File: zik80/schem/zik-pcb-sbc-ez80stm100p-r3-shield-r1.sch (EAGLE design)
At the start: 7 parts

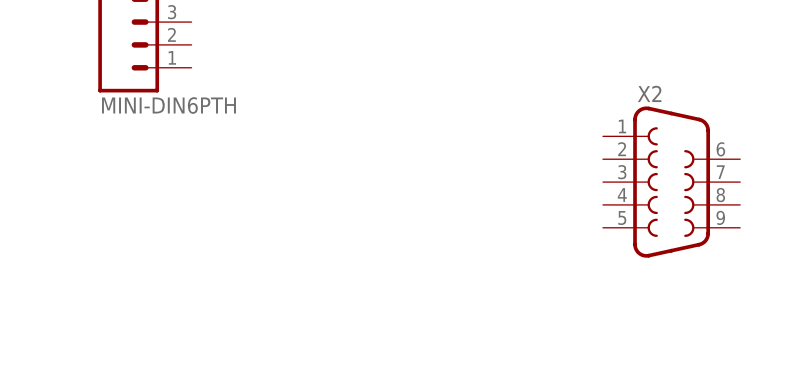
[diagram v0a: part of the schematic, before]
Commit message: Updated headphone part
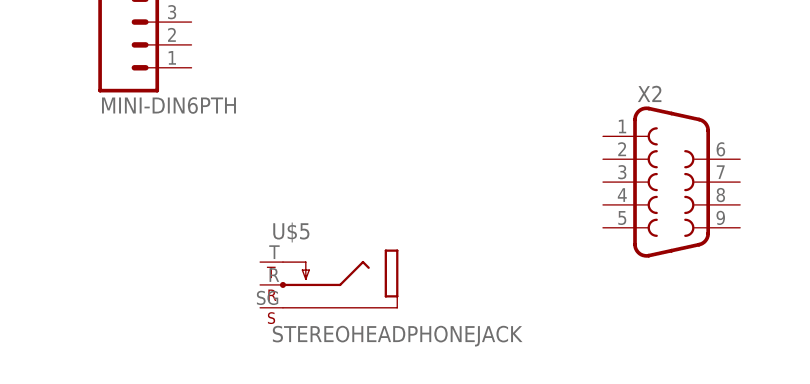
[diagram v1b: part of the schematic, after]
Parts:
- added U$5: STEREOHEADPHONEJACK, skeezix:STEREOHEADPHONEJACK
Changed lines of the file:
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@@
 <layer number="57" name="tCAD" color="10" fill="1" visible="no" active="no"/>
 <layer number="58" name="bCAD" color="11" fill="1" visible="no" active="no"/>
+<layer number="59" name="tCarbon" color="7" fill="1" visible="no" active="no"/>
+<layer number="60" name="bCarbon" color="7" fill="1" visible="no" active="no"/>
+<layer number="90" name="Modules" color="7" fill="1" visible="no" active="yes"/>
 <layer number="91" name="Nets" color="2" fill="1" visible="yes" active="yes"/>
 <layer number="92" name="Busses" color="1" fill="1" visible="yes" active="yes"/>
@@
 <layer number="127" name="_tValues" color="7" fill="1" visible="yes" active="yes"/>
 <layer number="128" name="_bValues" color="7" fill="1" visible="yes" active="yes"/>
+<layer number="129" name="Mask" color="7" fill="1" visible="yes" active="yes"/>
 <layer number="131" name="prix" color="7" fill="1" visible="yes" active="yes"/>
 <layer number="132" name="test" color="7" fill="1" visible="yes" active="yes"/>
@@
 <layer number="223" name="223bmp" color="24" fill="1" visible="no" active="no"/>
 <layer number="224" name="224bmp" color="25" fill="1" visible="no" active="no"/>
+<layer number="225" name="225bmp" color="7" fill="1" visible="yes" active="yes"/>
+<layer number="226" name="226bmp" color="7" fill="1" visible="yes" active="yes"/>
+<layer number="227" name="227bmp" color="7" fill="1" visible="yes" active="yes"/>
+<layer number="228" name="228bmp" color="7" fill="1" visible="yes" active="yes"/>
+<layer number="229" name="229bmp" color="7" fill="1" visible="yes" active="yes"/>
+<layer number="230" name="230bmp" color="7" fill="1" visible="yes" active="yes"/>
 <layer number="231" name="Eagle3D_PG1" color="7" fill="1" visible="yes" active="yes"/>
 <layer number="232" name="Eagle3D_PG2" color="7" fill="1" visible="yes" active="yes"/>
@@
 <layer number="251" name="SMDround" color="12" fill="11" visible="no" active="no"/>
 <layer number="254" name="cooling" color="7" fill="1" visible="yes" active="yes"/>
+<layer number="255" name="routoute" color="7" fill="1" visible="yes" active="yes"/>
 </layers>
 <schematic xreflabel="%F%N/%S.%C%R" xrefpart="/%S.%C%R">
@@
 <part name="VGA1" library="VideoConnectors-skeemod" deviceset="VGA-*" device="F90B"/>
 <part name="X1" library="adafruit-musb-skeemod" deviceset="USB" device="MICRO_20329"/>
+<part name="U$5" library="skeezix" deviceset="STEREOHEADPHONEJACK" device=""/>
 </parts>
 <sheets>
@@
 <instance part="VGA1" gate="G$1" x="157.48" y="66.04"/>
 <instance part="X1" gate="G$1" x="38.1" y="66.04"/>
+<instance part="U$5" gate="G$1" x="101.6" y="-7.62"/>
 </instances>
 <busses>
@@
 </schematic>
 </drawing>
+<compatibility>
+<note version="6.3" minversion="6.2.2" severity="warning">
+Since Version 6.2.2 text objects can contain more than one line,
+which will not be processed correctly with this version.
+</note>
+</compatibility>
 </eagle>

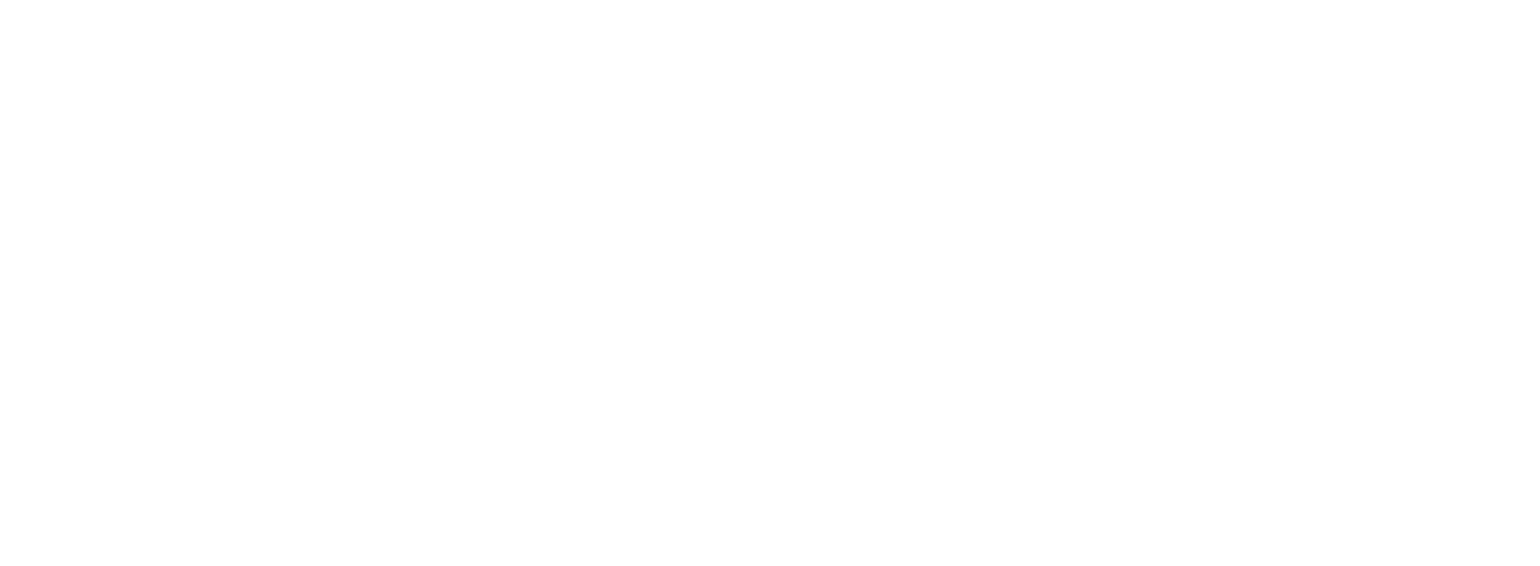
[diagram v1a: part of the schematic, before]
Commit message: Dropped TPS7133QP and FTDI onto shield start
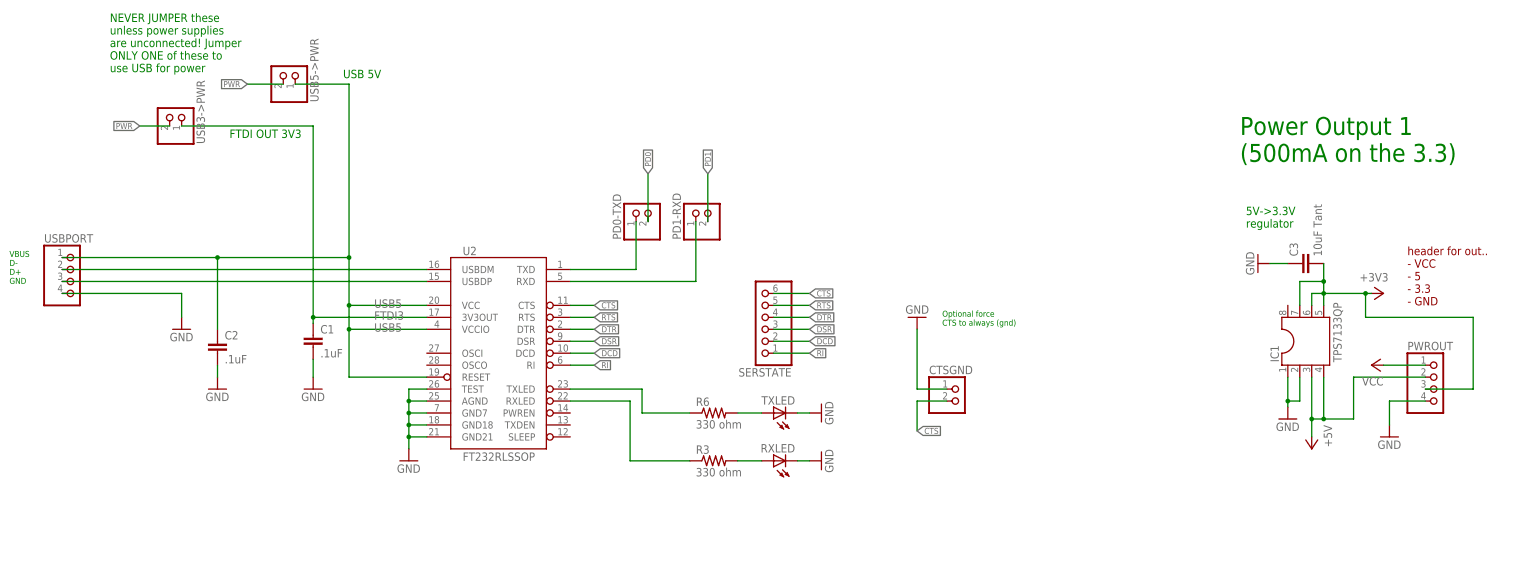
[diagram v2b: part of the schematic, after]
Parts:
- added C1, C2: .1uF, rcl:C-EU025-025X050
- added C3: 10uF Tant, rcl:C-EU025-025X050
- added CTSGND, PD0-TXD, PD1-RXD, USB3->PWR, USB5->PWR: (no value), pinhead:PINHD-1X2
- added IC1: TPS7133QP, ic-package:DIL8
- added PWROUT, USBPORT: (no value), pinhead:PINHD-1X4
- added R3, R6: 330 ohm, rcl:R-US_0204/7
- added RXLED, TXLED: (no value), SparkFun-LED:LED5MM
- added SERSTATE: (no value), pinhead:PINHD-1X6
- added U2: FT232RLSSOP, SparkFun:FT232RLSSOP
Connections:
- new net +3V3: C3.2, IC1.5, IC1.6, IC1.7, PWROUT.3
- new net +5V: IC1.3, IC1.4, PWROUT.2
- new net CTS: CTSGND.2, SERSTATE.6, U2.CTS
- new net DCD: SERSTATE.2, U2.DCD
- new net DSR: SERSTATE.3, U2.DSR
- new net DTR: SERSTATE.4, U2.DTR
- new net FTDI3: C1.1, U2.3V3OUT, USB3->PWR.1
- new net GND: C1.2, C2.2, C3.1, CTSGND.1, IC1.1, IC1.2, PWROUT.4, RXLED.C, TXLED.C, U2.AGND, U2.GND18, U2.GND21, U2.GND7, U2.TEST, USBPORT.4
- new net N$10: R3.2, RXLED.A
- new net N$11: R3.1, U2.RXLED
- new net N$12: PD0-TXD.1, U2.TXD
- new net N$13: PD1-RXD.1, U2.RXD
- new net N$4: R6.2, TXLED.A
- new net N$8: R6.1, U2.TXLED
- new net PD0: PD0-TXD.2
- new net PD1: PD1-RXD.2
- new net PWR: USB3->PWR.2, USB5->PWR.2
- new net RI: SERSTATE.1, U2.RI
- new net RTS: SERSTATE.5, U2.RTS
- new net USB5: C2.1, U2.RESET, U2.VCC, U2.VCCIO, USB5->PWR.1, USBPORT.1
- new net USB_D+: U2.USBDP, USBPORT.3
- new net USB_D-: U2.USBDM, USBPORT.2
- new net VCC: PWROUT.1
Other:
- note added: "5V->3.3V regulator"
- note added: "FTDI OUT 3V3"
- note added: "NEVER JUMPER these unless power supplies are unconnected! Jumper ONLY ONE of these to use USB for power"
- note added: "Optional force CTS to always (gnd)"
- note added: "Power Output 1 (500mA on the 3.3)"
- note added: "USB 5V"
- note added: "VBUS D- D+ GND"
- note added: "header for out.. - VCC - 5 - 3.3 - GND"

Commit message: shield progress.. about 50%? pcb coming together, working on placement. Schem has most or everything, just need to hook it all up.
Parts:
- removed X1: (no value), adafruit-musb-skeemod:USBMICRO_20329
- removed X2: (no value), SparkFun-Connectors-skeemod:DB9FEMALE
- added 3V3OUT, 5OUT, GNDOUT: (no value), pinhead:PINHD-1X3
- added BOB-PA: (no value), pinhead:PINHD-1X16
- added BOBGPIOB, GPIOC-JOY0, GPIOD-JOY1: (no value), pinhead:PINHD-1X8
- added C23: 100uF, rcl:C-EU025-025X050
- added C25: 250uF Pol, rcl:CPOL-USE3.5-8
- added C26: .05uF, rcl:C-EU025-025X050
- added JOY0, JOY1: (no value), SparkFun-Connectors-skeemod:DB9FEMALE
- added LINEOUT: (no value), pinhead:PINHD-1X2
- added PS2KEYB, PWRIN, SPKR: (no value), pinhead:PINHD-1X4
- added R34: 1K, rcl:R-US_0204/7
- added R37: 10, rcl:R-US_0204/7
- added U$6: LM386-DIP, skeezix:LM386-DIP
- added USBGPU, USBSERPWR: (no value), adafruit-musb-skeemod:USBMICRO_20329
- added VGAHDR: (no value), pinhead:PINHD-1X6
- renumbered PD0-TXD to ZPD1-TXD, PD1-RXD to ZPD0-RXD, USB3->PWR to FT3V3->PWR3, USB5->PWR to FT5V->PWR5
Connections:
- removed net +3V3: C3.2, IC1.5, IC1.6, IC1.7, PWROUT.3
- removed net PD0: ZPD1-TXD.2
- removed net PD1: ZPD0-RXD.2
- removed net PWR: FT3V3->PWR3.2, FT5V->PWR5.2
- new net N$1: C23.2, U$3.CCW
- new net N$2: U$3.LO, U$6.3
- new net N$22: C25.+, C26.2, U$6.5
- new net N$23: C25.-
- new net N$24: C26.1, R37.2
- new net N$3: LINEOUT.2, U$6.7
- new net N$6: C23.1, R34.1, SPKR.1, SPKR.2, SPKR.3
- new net PWR3: 3V3OUT.1, 3V3OUT.2, 3V3OUT.3, C3.2, FT3V3->PWR3.2, IC1.5, IC1.6, IC1.7, PWRIN.3, PWROUT.3
- new net PWR5: 5OUT.1, 5OUT.2, 5OUT.3, FT5V->PWR5.2, IC1.3, IC1.4, PWRIN.2, PWROUT.2, U$1.VCC
- new net SPA0: BOB-PA.1
- new net SPA10: BOB-PA.11
- new net SPA11: BOB-PA.12, USBGPU.D-
- new net SPA12: BOB-PA.13, USBGPU.D+
- new net ZPB0: BOBGPIOB.1
- new net ZPB2-SS: BOBGPIOB.3
- new net ZPB3-SCK: BOBGPIOB.4
- new net ZPB6-MISO: BOBGPIOB.7
- new net ZPB7-MOSI: BOBGPIOB.8
- new net ZPD0: GPIOD-JOY1.1, ZPD0-RXD.2
- new net ZPD1: GPIOD-JOY1.2, ZPD1-TXD.2
- new net ZPD6: GPIOD-JOY1.7
- new net ZPD7: GPIOD-JOY1.8
- net +5V: now also U$6.6, USBGPU.VBUS; no longer IC1.3, IC1.4, PWROUT.2
- net GND: now also GNDOUT.1, GNDOUT.2, GNDOUT.3, LINEOUT.1, PWRIN.4, R34.2, R37.1, U$1.GND, U$3.CW, U$6.2, U$6.4, USBGPU.GND, USBSERPWR.GND
- net USB5: now also USBSERPWR.VBUS
- net USB_D+: now also USBSERPWR.D-
- net USB_D-: now also USBSERPWR.D+
- net VCC: now also PWRIN.1
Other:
- note added: "- NEVER JUMPER enable these unless barrel power jack or headers are unconnected! - Jumper ONLY ONE of these to use USB for power"
- note added: "Audio Amp"
- note added: "FTDI RX -> mcu TX"
- note added: "FTDI TX -> mcu RX"
- note added: "OTG_FS_ID OTG_FS_DM OTG_FS_DP"
- note added: "One of: - USB jack, then jumper enable 5v (populated TPS7133) - USB jack, jumper enable 5v and 3v3v (unpopulated TPS7133); pray FTDI can supply enough amp on 3V line - Barrel jack with 5V input brick (populated TPS7133) .. needs TPS - PWRIN header with VCC, 5V, 3V3, GND (unpopulated TPS7133) .. circumvents TPS"
- note added: "Power Block"
- note added: "Powering PCB Notes"
- note added: "Use Vcc12V or +5? Decouple Vcc/GND with a cap?"
- note added: "VCC 5V 3V3 GND"
- note added: "Verify - all pin1 orientations! - which jacks can be used, while in middle of pcb - jacks in middle have clearance for SD-pulling, headphone pulling, etc - ensure cap, resistor sizine/type - printout pcb to printer, eyeball it - PWR v PW% vs PWR3 vs 5V vs etc .. all powers are hooked right - net review; ensure no +5V and other old net names - uncover reset buttons.. anything else? LEDs? - verify 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"
- note added: "joy up (z80 tx0) joy down (zip rx0) joy left joy right joy fire GND (unused i think actually) ps2 clk ps2 data"
- note added: "joy up joy down joy left joy right joy fire unused I think vblank in frame rdy out"
- note added: "todo: headphone jack"
- note removed: "NEVER JUMPER these unless power supplies are unconnected! Jumper ONLY ONE of these to use USB for power"
- note removed: "Power Output 1 (500mA on the 3.3)"
- moved on the sheet: C3, IC1, PWROUT, U$4, U$5, VGA1G$1

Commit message: shield - Some placement progress
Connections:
- net +5V: no longer USBGPU.VBUS
- net PWR5: now also USBGPU.VBUS
- net SPA11: now also USBGPU.D+; no longer USBGPU.D-
- net SPA12: now also USBGPU.D-; no longer USBGPU.D+
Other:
- note added: "Schem lib is mislabeled? Shoudl be minus always close to V?"
- moved on the sheet: USBGPU
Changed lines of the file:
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@@
 - verify USB 5p is correct .. power and D- D+ correct pins
 - potwheel on right? cmp to r4
-- mill in some slots for air flow? visibility?</text>
+- mill in some slots for air flow? visibility?
+- silkscreen name/branding/rev
+- data USB
+- SD, unrouted, DRC, ERC...
+- extra BoB pins? i2c? SPI? all that stuff, bring them up and dont populate?
+- Ensure slot for cart is deep enough for plastic box clearance?
+- case readyness?</text>
 <text x="114.3" y="-119.38" size="2.54" layer="91">Use Vcc12V or +5?
 Decouple Vcc/GND with a cap?</text>
@@
 OTG_FS_DM
 OTG_FS_DP</text>
+<text x="-27.94" y="160.02" size="1.778" layer="91">Schem lib is mislabeled?
+Shoudl be minus always
+close to V?</text>
+<text x="494.03" y="-17.78" size="1.778" layer="91">Schem lib is mislabeled?
+Shoudl be minus always
+close to V?</text>
 </plain>
 <instances>
@@
 <instance part="+3V2" gate="G$1" x="281.94" y="124.46" rot="R180"/>
 <instance part="P+3" gate="1" x="308.61" y="124.46" rot="R180"/>
-<instance part="USBGPU" gate="G$1" x="502.92" y="2.54" rot="MR0"/>
-<instance part="GND13" gate="1" x="488.95" y="-15.24"/>
-<instance part="P+4" gate="1" x="488.95" y="21.59"/>
+<instance part="USBGPU" gate="G$1" x="500.38" y="0" rot="MR0"/>
+<instance part="GND13" gate="1" x="485.14" y="-17.78"/>
+<instance part="P+4" gate="1" x="485.14" y="19.05"/>
 </instances>
 <busses>
@@
 <segment>
 <pinref part="USBGPU" gate="G$1" pin="GND"/>
-<wire x1="492.76" y1="-2.54" x2="488.95" y2="-2.54" width="0.1524" layer="91"/>
-<wire x1="488.95" y1="-2.54" x2="488.95" y2="-12.7" width="0.1524" layer="91"/>
+<wire x1="490.22" y1="-5.08" x2="485.14" y2="-5.08" width="0.1524" layer="91"/>
+<wire x1="485.14" y1="-5.08" x2="485.14" y2="-15.24" width="0.1524" layer="91"/>
 <pinref part="GND13" gate="1" pin="GND"/>
 </segment>
@@
 <pinref part="+5V2" gate="1" pin="+5V"/>
 </segment>
-<segment>
-<pinref part="USBGPU" gate="G$1" pin="VBUS"/>
-<wire x1="492.76" y1="7.62" x2="488.95" y2="7.62" width="0.1524" layer="91"/>
-<wire x1="488.95" y1="7.62" x2="488.95" y2="19.05" width="0.1524" layer="91"/>
-<pinref part="P+4" gate="1" pin="+5V"/>
-</segment>
 </net>
 <net name="VCC" class="0">
@@
 <pinref part="P+3" gate="1" pin="+5V"/>
 </segment>
+<segment>
+<pinref part="USBGPU" gate="G$1" pin="VBUS"/>
+<wire x1="490.22" y1="5.08" x2="485.14" y2="5.08" width="0.1524" layer="91"/>
+<wire x1="485.14" y1="5.08" x2="485.14" y2="16.51" width="0.1524" layer="91"/>
+<pinref part="P+4" gate="1" pin="+5V"/>
+</segment>
 </net>
 <net name="ZPD0" class="0">
@@
 <wire x1="471.17" y1="2.54" x2="462.28" y2="2.54" width="0.1524" layer="91"/>
 <label x="462.28" y="2.54" size="1.27" layer="95" rot="R180" xref="yes"/>
-<pinref part="USBGPU" gate="G$1" pin="D-"/>
-<wire x1="471.17" y1="2.54" x2="492.76" y2="2.54" width="0.1524" layer="91"/>
+<pinref part="USBGPU" gate="G$1" pin="D+"/>
+<wire x1="471.17" y1="2.54" x2="490.22" y2="2.54" width="0.1524" layer="91"/>
 </segment>
 </net>
@@
 <wire x1="471.17" y1="0" x2="462.28" y2="0" width="0.1524" layer="91"/>
 <label x="462.28" y="0" size="1.27" layer="95" rot="R180" xref="yes"/>
-<wire x1="471.17" y1="0" x2="486.41" y2="0" width="0.1524" layer="91"/>
-<wire x1="486.41" y1="0" x2="486.41" y2="5.08" width="0.1524" layer="91"/>
-<pinref part="USBGPU" gate="G$1" pin="D+"/>
-<wire x1="486.41" y1="5.08" x2="492.76" y2="5.08" width="0.1524" layer="91"/>
-</segment>
-</net>
+<wire x1="471.17" y1="0" x2="490.22" y2="0" width="0.1524" layer="91"/>
+<pinref part="USBGPU" gate="G$1" pin="D-"/>
+</segment>
+</net>
